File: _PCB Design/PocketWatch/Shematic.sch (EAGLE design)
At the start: 55 parts, among them U2 ATTINY88-AU

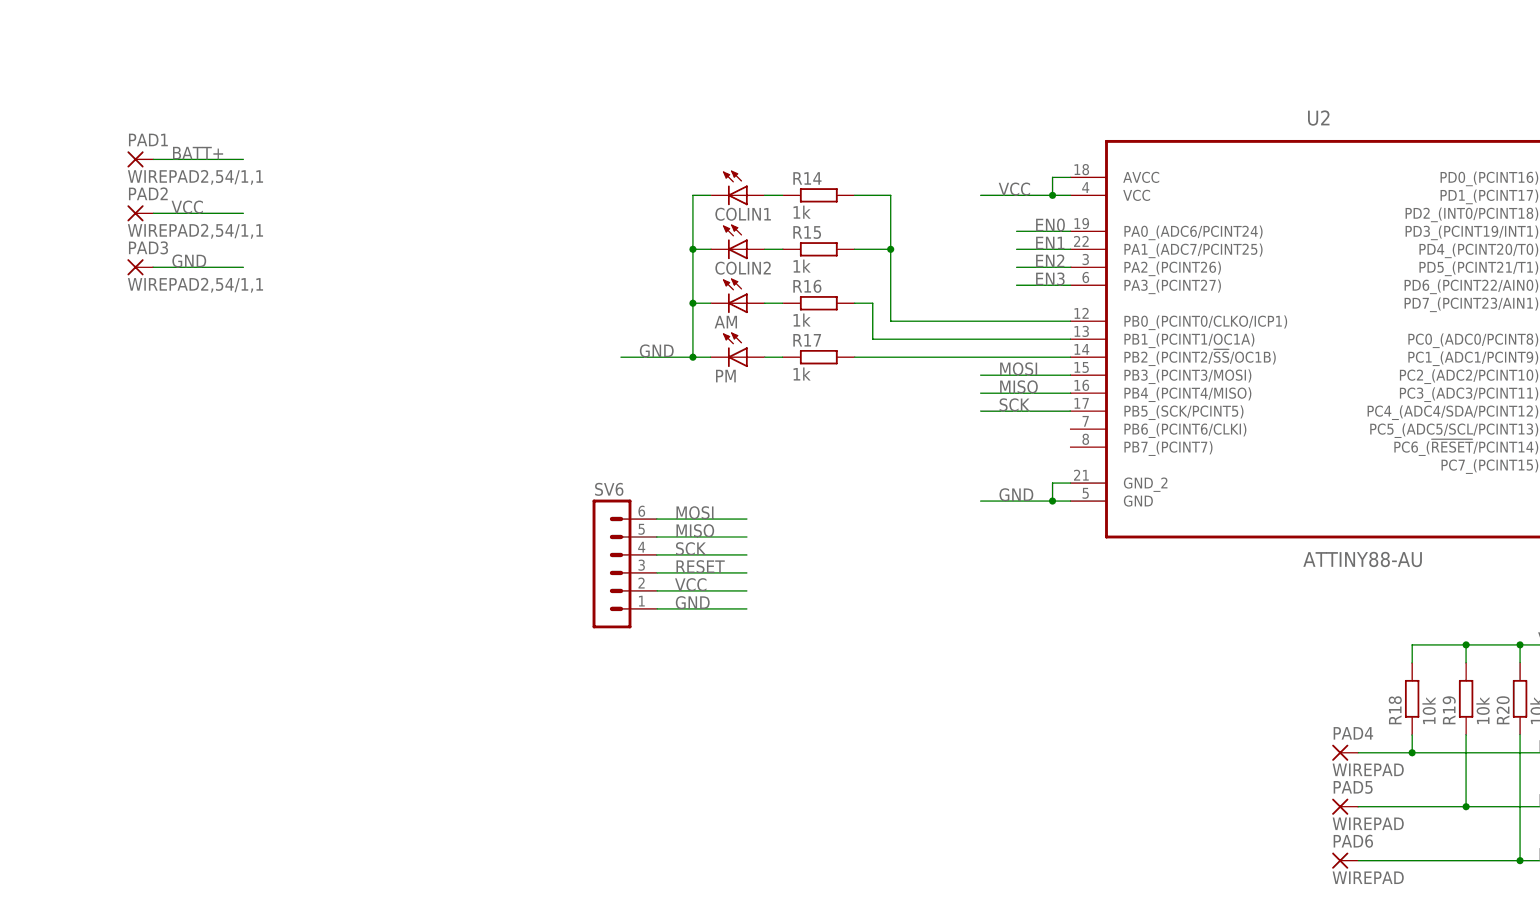
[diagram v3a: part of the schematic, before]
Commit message: Re-routed tube board with thicker traces. Improved 3rd party board dimension accuracy.
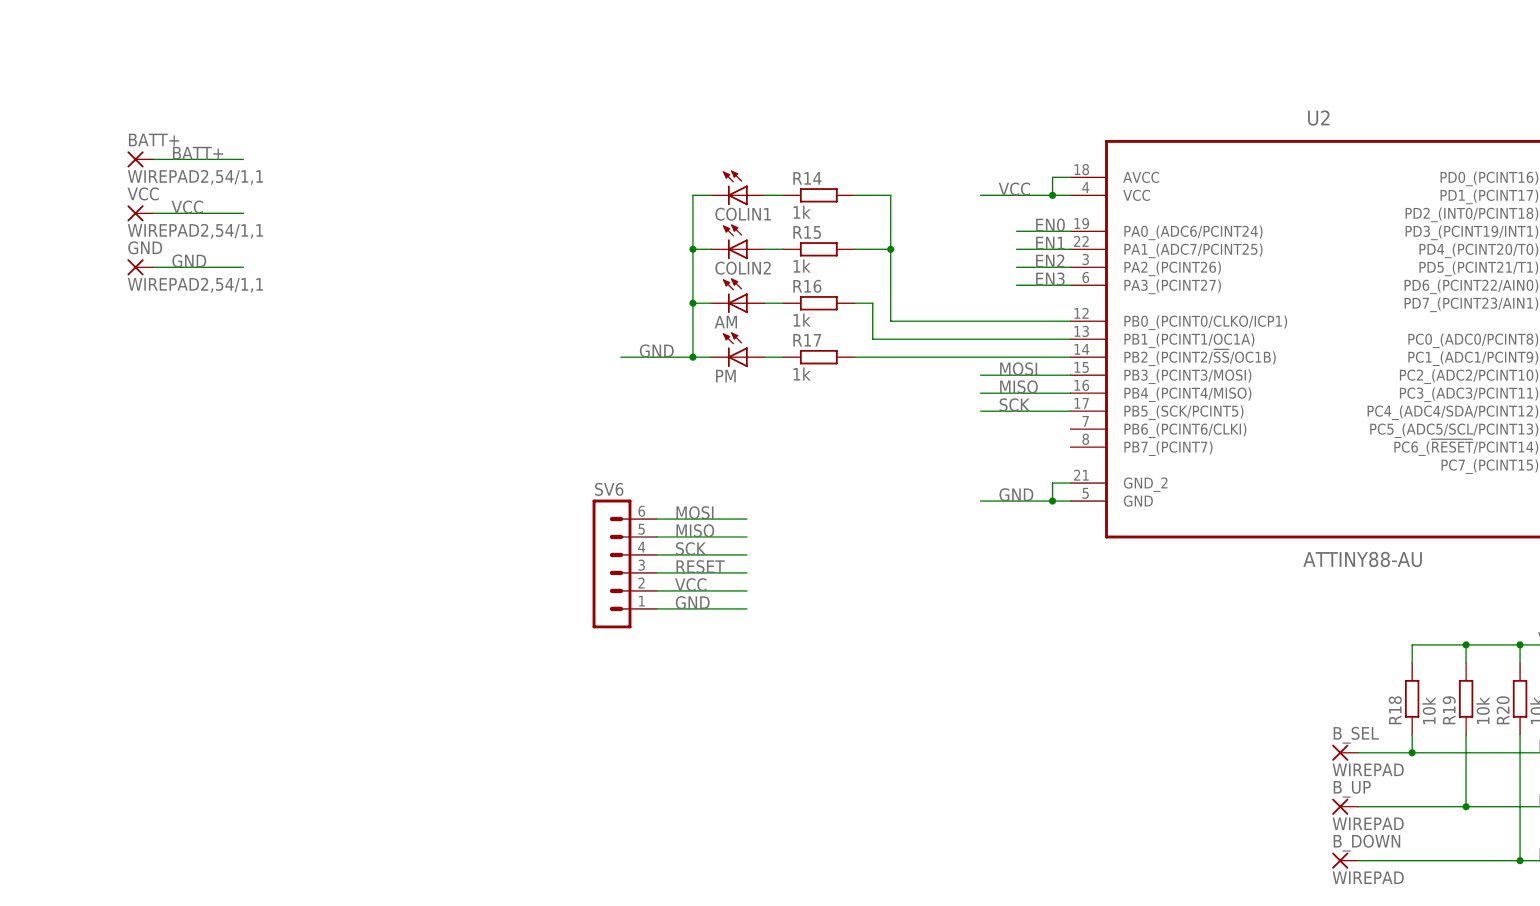
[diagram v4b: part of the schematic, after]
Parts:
- renumbered PAD1 to BATT+, PAD2 to VCC, PAD3 to GND, PAD4 to B_SEL, PAD5 to B_UP, PAD6 to B_DOWN
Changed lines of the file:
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@@
 <part name="6PF" library="Library" deviceset="CFS206" device=""/>
 <part name="C2" library="eagle-ltspice" library_urn="urn:adsk.eagle:library:217" deviceset="C" device="C1206" package3d_urn="urn:adsk.eagle:package:13279/1" value="12pF"/>
-<part name="PAD1" library="wirepad" library_urn="urn:adsk.eagle:library:412" deviceset="WIREPAD" device="2,54/1,1" package3d_urn="urn:adsk.eagle:package:30836/1"/>
+<part name="BATT+" library="wirepad" library_urn="urn:adsk.eagle:library:412" deviceset="WIREPAD" device="2,54/1,1" package3d_urn="urn:adsk.eagle:package:30836/1"/>
 <part name="SV1" library="con-lstb" library_urn="urn:adsk.eagle:library:162" deviceset="MA08-1" device="" package3d_urn="urn:adsk.eagle:package:8343/1"/>
 <part name="SV3" library="con-lstb" library_urn="urn:adsk.eagle:library:162" deviceset="MA04-1" device="" package3d_urn="urn:adsk.eagle:package:8337/1"/>
@@
 <part name="C9" library="eagle-ltspice" library_urn="urn:adsk.eagle:library:217" deviceset="C" device="C1206" package3d_urn="urn:adsk.eagle:package:13279/1" value="220uF"/>
 <part name="C10" library="eagle-ltspice" library_urn="urn:adsk.eagle:library:217" deviceset="C" device="C1206" package3d_urn="urn:adsk.eagle:package:13279/1" value="1uF"/>
-<part name="PAD2" library="wirepad" library_urn="urn:adsk.eagle:library:412" deviceset="WIREPAD" device="2,54/1,1" package3d_urn="urn:adsk.eagle:package:30836/1"/>
-<part name="PAD3" library="wirepad" library_urn="urn:adsk.eagle:library:412" deviceset="WIREPAD" device="2,54/1,1" package3d_urn="urn:adsk.eagle:package:30836/1"/>
+<part name="VCC" library="wirepad" library_urn="urn:adsk.eagle:library:412" deviceset="WIREPAD" device="2,54/1,1" package3d_urn="urn:adsk.eagle:package:30836/1"/>
+<part name="GND" library="wirepad" library_urn="urn:adsk.eagle:library:412" deviceset="WIREPAD" device="2,54/1,1" package3d_urn="urn:adsk.eagle:package:30836/1"/>
 <part name="COLIN2" library="eagle-ltspice" library_urn="urn:adsk.eagle:library:217" deviceset="LED_E" device="LD260" package3d_urn="urn:adsk.eagle:package:13313/1"/>
-<part name="PAD4" library="wirepad" library_urn="urn:adsk.eagle:library:412" deviceset="WIREPAD" device="2,54/1,1" package3d_urn="urn:adsk.eagle:package:30836/1" value="WIREPAD"/>
-<part name="PAD5" library="wirepad" library_urn="urn:adsk.eagle:library:412" deviceset="WIREPAD" device="2,54/1,1" package3d_urn="urn:adsk.eagle:package:30836/1" value="WIREPAD"/>
-<part name="PAD6" library="wirepad" library_urn="urn:adsk.eagle:library:412" deviceset="WIREPAD" device="2,54/1,1" package3d_urn="urn:adsk.eagle:package:30836/1" value="WIREPAD"/>
+<part name="B_SEL" library="wirepad" library_urn="urn:adsk.eagle:library:412" deviceset="WIREPAD" device="2,54/1,1" package3d_urn="urn:adsk.eagle:package:30836/1" value="WIREPAD"/>
+<part name="B_UP" library="wirepad" library_urn="urn:adsk.eagle:library:412" deviceset="WIREPAD" device="2,54/1,1" package3d_urn="urn:adsk.eagle:package:30836/1" value="WIREPAD"/>
+<part name="B_DOWN" library="wirepad" library_urn="urn:adsk.eagle:library:412" deviceset="WIREPAD" device="2,54/1,1" package3d_urn="urn:adsk.eagle:package:30836/1" value="WIREPAD"/>
 <part name="AM" library="eagle-ltspice" library_urn="urn:adsk.eagle:library:217" deviceset="LED_E" device="LD260" package3d_urn="urn:adsk.eagle:package:13313/1"/>
 <part name="PM" library="eagle-ltspice" library_urn="urn:adsk.eagle:library:217" deviceset="LED_E" device="LD260" package3d_urn="urn:adsk.eagle:package:13313/1"/>
@@
 <instance part="6PF" gate="A" x="45.72" y="73.66" rot="R270"/>
 <instance part="C2" gate="G$1" x="33.02" y="81.28" rot="R270"/>
-<instance part="PAD1" gate="G$1" x="-104.14" y="20.32"/>
+<instance part="BATT+" gate="G$1" x="-104.14" y="20.32"/>
 <instance part="SV1" gate="1" x="124.46" y="10.16" rot="R180"/>
 <instance part="SV3" gate="1" x="162.56" y="20.32"/>
@@
 <instance part="C9" gate="G$1" x="-17.78" y="76.2"/>
 <instance part="C10" gate="G$1" x="-27.94" y="76.2"/>
-<instance part="PAD2" gate="G$1" x="-104.14" y="12.7"/>
-<instance part="PAD3" gate="G$1" x="-104.14" y="5.08"/>
+<instance part="VCC" gate="G$1" x="-104.14" y="12.7"/>
+<instance part="GND" gate="G$1" x="-104.14" y="5.08"/>
 <instance part="COLIN2" gate="G$1" x="-17.78" y="7.62" rot="R270"/>
-<instance part="PAD4" gate="G$1" x="66.04" y="-63.5"/>
-<instance part="PAD5" gate="G$1" x="66.04" y="-71.12"/>
-<instance part="PAD6" gate="G$1" x="66.04" y="-78.74"/>
+<instance part="B_SEL" gate="G$1" x="66.04" y="-63.5"/>
+<instance part="B_UP" gate="G$1" x="66.04" y="-71.12"/>
+<instance part="B_DOWN" gate="G$1" x="66.04" y="-78.74"/>
 <instance part="AM" gate="G$1" x="-17.78" y="0" rot="R270"/>
 <instance part="PM" gate="G$1" x="-17.78" y="-7.62" rot="R270"/>
@@
 </segment>
 <segment>
-<pinref part="PAD3" gate="G$1" pin="P"/>
+<pinref part="GND" gate="G$1" pin="P"/>
 <wire x1="-101.6" y1="5.08" x2="-88.9" y2="5.08" width="0.1524" layer="91"/>
 <label x="-99.06" y="5.08" size="1.778" layer="95"/>
@@
 </segment>
 <segment>
-<pinref part="PAD2" gate="G$1" pin="P"/>
+<pinref part="VCC" gate="G$1" pin="P"/>
 <wire x1="-101.6" y1="12.7" x2="-88.9" y2="12.7" width="0.1524" layer="91"/>
 <label x="-99.06" y="12.7" size="1.778" layer="95"/>
@@
 </segment>
 <segment>
-<pinref part="PAD1" gate="G$1" pin="P"/>
+<pinref part="BATT+" gate="G$1" pin="P"/>
 <wire x1="-101.6" y1="20.32" x2="-88.9" y2="20.32" width="0.1524" layer="91"/>
 <label x="-99.06" y="20.32" size="1.778" layer="95"/>
@@
 </segment>
 <segment>
-<pinref part="PAD4" gate="G$1" pin="P"/>
+<pinref part="B_SEL" gate="G$1" pin="P"/>
 <pinref part="R18" gate="G$1" pin="1"/>
 <wire x1="68.58" y1="-63.5" x2="76.2" y2="-63.5" width="0.1524" layer="91"/>
@@
 </segment>
 <segment>
-<pinref part="PAD5" gate="G$1" pin="P"/>
+<pinref part="B_UP" gate="G$1" pin="P"/>
 <pinref part="R19" gate="G$1" pin="1"/>
 <wire x1="68.58" y1="-71.12" x2="83.82" y2="-71.12" width="0.1524" layer="91"/>
@@
 </segment>
 <segment>
-<pinref part="PAD6" gate="G$1" pin="P"/>
+<pinref part="B_DOWN" gate="G$1" pin="P"/>
 <pinref part="R20" gate="G$1" pin="1"/>
 <wire x1="68.58" y1="-78.74" x2="91.44" y2="-78.74" width="0.1524" layer="91"/>

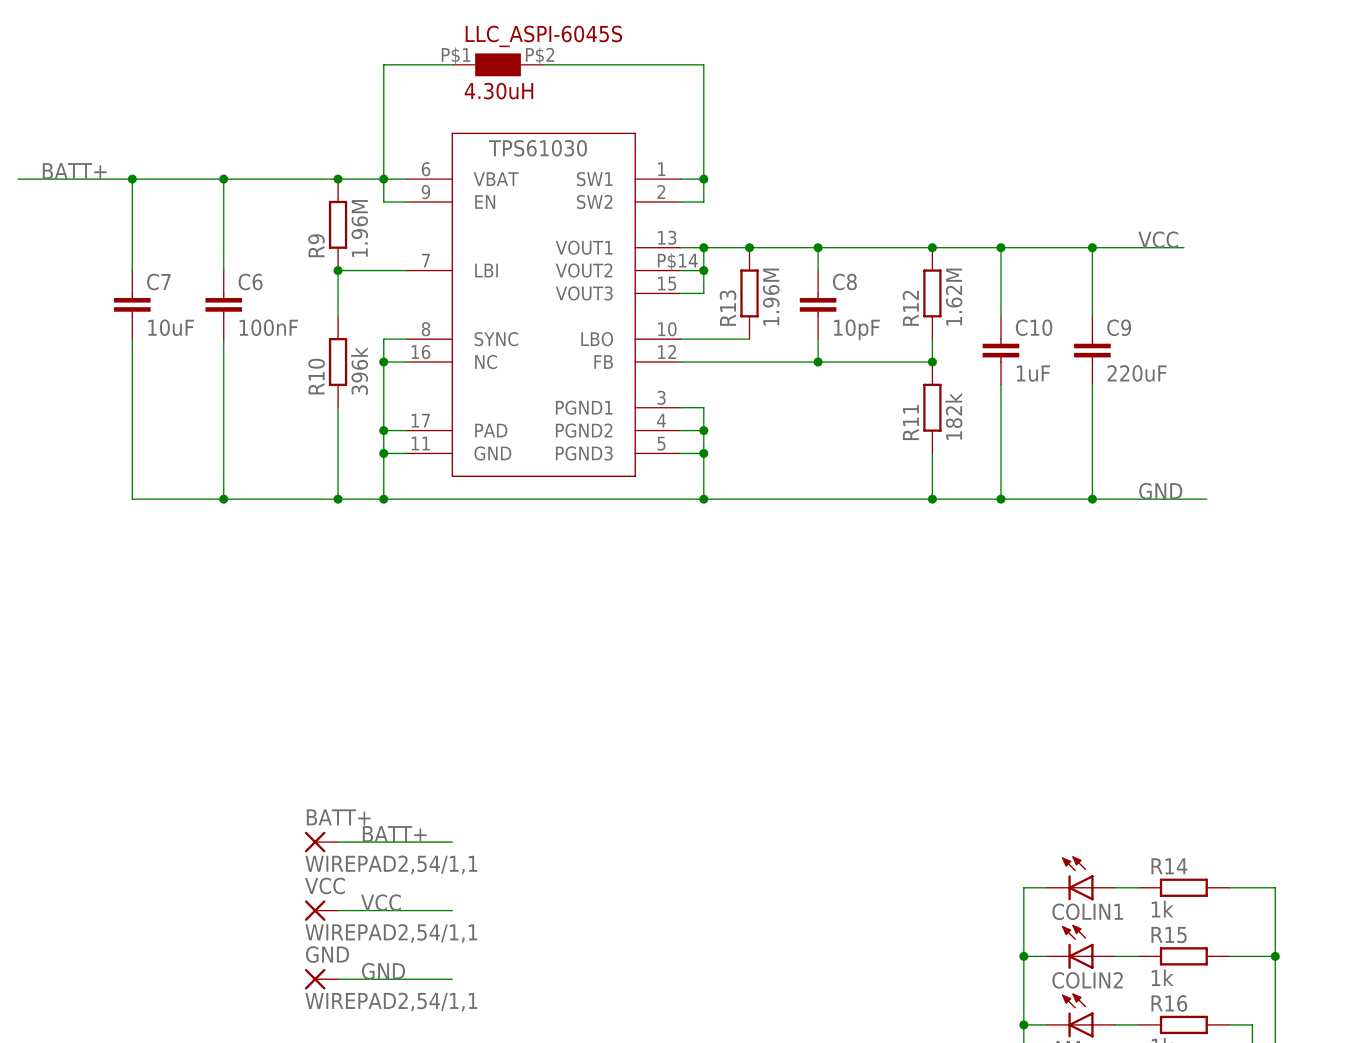
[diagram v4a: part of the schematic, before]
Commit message: Removed 1st party boost converter.
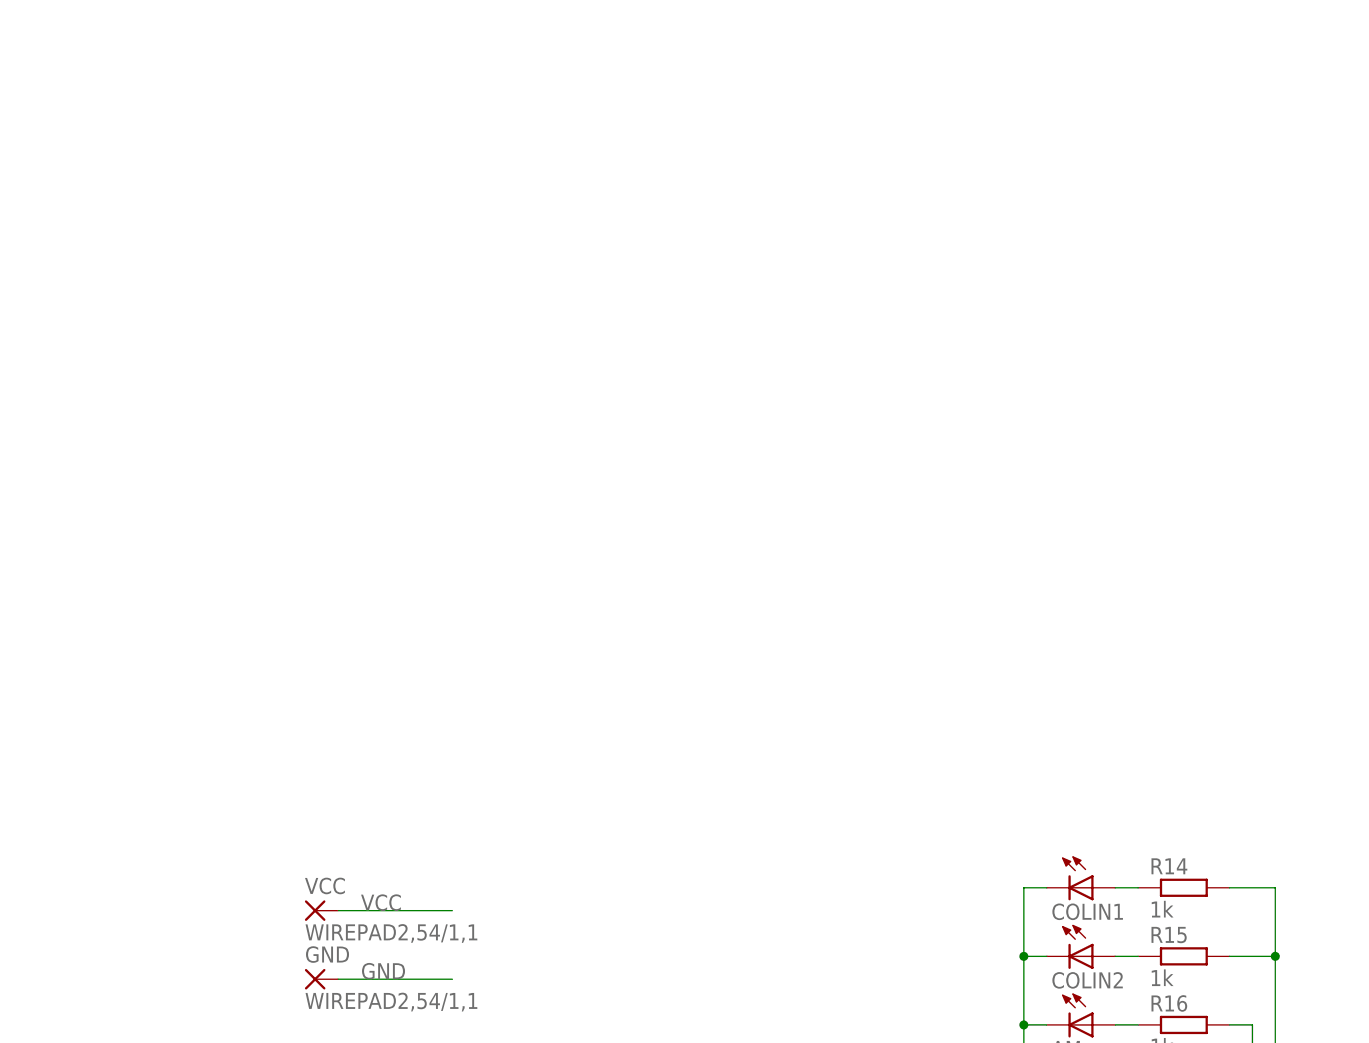
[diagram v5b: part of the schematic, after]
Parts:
- removed BATT+: WIREPAD2,54/1,1, wirepad:WIREPAD2,54/1,1
- removed C10: 1uF, eagle-ltspice:CC1206
- removed C6: 100nF, eagle-ltspice:CC1206
- removed C7: 10uF, eagle-ltspice:CC1206
- removed C8: 10pF, eagle-ltspice:CC1206
- removed C9: 220uF, eagle-ltspice:CC1206
- removed LLC_ASPI-6045S: 4.30uH, Library:LLC_ASPI-6045S
- removed R10: 396k, eagle-ltspice:RR1206
- removed R11: 182k, eagle-ltspice:RR1206
- removed R12: 1.62M, eagle-ltspice:RR1206
- removed R13, R9: 1.96M, eagle-ltspice:RR1206
- removed U$6: TPS61030, Library:TPS61030
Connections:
- removed net BATT+: BATT+.P, C6.1, C7.1, LLC_ASPI-6045S.P$1, R9.2, U$6.EN, U$6.VBAT
- removed net N$10: R13.1, U$6.LBO
- removed net N$11: R10.2, R9.1, U$6.LBI
- removed net N$13: C8.2, R11.2, R12.1, U$6.FB
- removed net N$8: LLC_ASPI-6045S.P$2, U$6.SW1, U$6.SW2
- net GND: no longer C10.2, C6.2, C7.2, C9.2, R10.1, R11.1, U$6.GND, U$6.NC, U$6.PAD, U$6.PGND1, U$6.PGND2, U$6.PGND3, U$6.SYNC
- net VCC: no longer C10.1, C8.1, C9.1, R12.2, R13.2, U$6.VOUT1, U$6.VOUT2, U$6.VOUT3

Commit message: Update
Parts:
- added TGND, TGND2: WIREPAD2,54/1,1, wirepad:WIREPAD2,54/1,1
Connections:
- new net TGND: TGND.P
- net GND: now also TGND2.P
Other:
- moved on the sheet: GND, VCC
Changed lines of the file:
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@@
 <part name="R8" library="eagle-ltspice" library_urn="urn:adsk.eagle:library:217" deviceset="R" device="R1206" package3d_urn="urn:adsk.eagle:package:13301/1" value="1k"/>
 <part name="VCC" library="wirepad" library_urn="urn:adsk.eagle:library:412" deviceset="WIREPAD" device="2,54/1,1" package3d_urn="urn:adsk.eagle:package:30836/1"/>
-<part name="GND" library="wirepad" library_urn="urn:adsk.eagle:library:412" deviceset="WIREPAD" device="2,54/1,1" package3d_urn="urn:adsk.eagle:package:30836/1"/>
 <part name="COLIN2" library="eagle-ltspice" library_urn="urn:adsk.eagle:library:217" deviceset="LED_E" device="LD260" package3d_urn="urn:adsk.eagle:package:13313/1"/>
 <part name="B_SEL" library="wirepad" library_urn="urn:adsk.eagle:library:412" deviceset="WIREPAD" device="2,54/1,1" package3d_urn="urn:adsk.eagle:package:30836/1" value="WIREPAD"/>
@@
 <part name="R20" library="eagle-ltspice" library_urn="urn:adsk.eagle:library:217" deviceset="R" device="R1206" package3d_urn="urn:adsk.eagle:package:13301/1" value="10k"/>
 <part name="U$5" library="Library" deviceset="COIN" device=""/>
+<part name="TGND" library="wirepad" library_urn="urn:adsk.eagle:library:412" deviceset="WIREPAD" device="2,54/1,1" package3d_urn="urn:adsk.eagle:package:30836/1"/>
+<part name="TGND2" library="wirepad" library_urn="urn:adsk.eagle:library:412" deviceset="WIREPAD" device="2,54/1,1" package3d_urn="urn:adsk.eagle:package:30836/1"/>
+<part name="GND" library="wirepad" library_urn="urn:adsk.eagle:library:412" deviceset="WIREPAD" device="2,54/1,1" package3d_urn="urn:adsk.eagle:package:30836/1"/>
 </parts>
 <sheets>
@@
 <instance part="R7" gate="G$1" x="266.7" y="-30.48" rot="R90"/>
 <instance part="R8" gate="G$1" x="299.72" y="-30.48" rot="R90"/>
-<instance part="VCC" gate="G$1" x="-104.14" y="12.7"/>
-<instance part="GND" gate="G$1" x="-104.14" y="5.08"/>
+<instance part="VCC" gate="G$1" x="-35.56" y="55.88"/>
 <instance part="COLIN2" gate="G$1" x="-17.78" y="7.62" rot="R270"/>
 <instance part="B_SEL" gate="G$1" x="66.04" y="-63.5"/>
@@
 <instance part="R20" gate="G$1" x="91.44" y="-55.88" rot="R90"/>
 <instance part="U$5" gate="G$1" x="88.9" y="55.88"/>
+<instance part="TGND" gate="G$1" x="162.56" y="7.62"/>
+<instance part="TGND2" gate="G$1" x="162.56" y="-30.48"/>
+<instance part="GND" gate="G$1" x="-35.56" y="48.26"/>
 </instances>
 <busses>
@@
 </segment>
 <segment>
+<wire x1="-33.02" y1="48.26" x2="-20.32" y2="48.26" width="0.1524" layer="91"/>
+<label x="-30.48" y="48.26" size="1.778" layer="95"/>
 <pinref part="GND" gate="G$1" pin="P"/>
-<wire x1="-101.6" y1="5.08" x2="-88.9" y2="5.08" width="0.1524" layer="91"/>
-<label x="-99.06" y="5.08" size="1.778" layer="95"/>
 </segment>
 <segment>
@@
 <label x="-33.02" y="-7.62" size="1.778" layer="95"/>
 </segment>
+<segment>
+<pinref part="TGND2" gate="G$1" pin="P"/>
+<wire x1="165.1" y1="-30.48" x2="175.26" y2="-30.48" width="0.1524" layer="91"/>
+<label x="167.64" y="-30.48" size="1.778" layer="95"/>
+</segment>
 </net>
 <net name="VCC" class="0">
@@
 <segment>
 <pinref part="VCC" gate="G$1" pin="P"/>
-<wire x1="-101.6" y1="12.7" x2="-88.9" y2="12.7" width="0.1524" layer="91"/>
-<label x="-99.06" y="12.7" size="1.778" layer="95"/>
+<wire x1="-33.02" y1="55.88" x2="-20.32" y2="55.88" width="0.1524" layer="91"/>
+<label x="-30.48" y="55.88" size="1.778" layer="95"/>
 </segment>
 <segment>
@@
 </segment>
 </net>
+<net name="TGND" class="0">
+<segment>
+<pinref part="TGND" gate="G$1" pin="P"/>
+<wire x1="165.1" y1="7.62" x2="175.26" y2="7.62" width="0.1524" layer="91"/>
+<label x="167.64" y="7.62" size="1.778" layer="95"/>
+</segment>
+</net>
